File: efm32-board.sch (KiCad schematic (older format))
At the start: 30 parts, among them J1 Conn_01x20, J2 Conn_01x20, J3 USB_OTG, J4 Conn_02x03_Odd_Even, J5 Conn_01x20, J6 Conn_01x20, SW1 reset, SW2 reset, U1 EFM32HG-48LQFP, U2 SPX3819M5-L-3-3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

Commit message: Add +5v input diode array for split vbus and vin
Signed-off-by: Martin Ribelotta <martinribelotta@gmail.com>
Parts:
- added D2: PMEG2005CT, TO_SOT_Packages_SMD:SOT-23, symbol D_Schottky_x2_KCom_AAK
- J4: footprint Pin_Headers:Pin_Header_Straight_2x03_Pitch2.54mm_SMD -> Pin_Headers:Pin_Header_Straight_2x03_Pitch2.54mm
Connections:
- net +5V: now also D2.3 (K); no longer J2.1 (Pin_1), J3.1 (VBUS), J5.1 (Pin_1)
- new net vin: D2.1 (A), J2.1 (Pin_1), J5.1 (Pin_1)
- new net vusb: D2.2 (A), J3.1 (VBUS)

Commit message: Corrections and fixeds
Signed-off-by: Martin Ribelotta <martinribelotta@gmail.com>
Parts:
- added C12: 4.7u, Capacitors_SMD:C_0603, symbol C_Small
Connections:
- net +3V3: no longer C7.1, U1.33 (USB_VREGI), U1.34 (USB_VREGO)
- net +5V: no longer J4.2 (Pin_2)
- net GND: now also C12.2
- net vusb: now also U1.33 (USB_VREGI), C12.1
- new net: C7.1, U1.34 (USB_VREGO)
- no-connect marks 3 -> 4
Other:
- moved on the sheet: C7
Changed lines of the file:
@@
 L GND #PWR012
 U 1 1 59CF2E8C
-P 6450 3125
-F 0 "#PWR012" H 6450 2875 50  0001 C CNN
-F 1 "GND" H 6455 2952 50  0000 C CNN
-F 2 "" H 6450 3125 50  0001 C CNN
-F 3 "" H 6450 3125 50  0001 C CNN
-	1    6450 3125
+P 7000 3150
+F 0 "#PWR012" H 7000 2900 50  0001 C CNN
+F 1 "GND" H 7005 2977 50  0000 C CNN
+F 2 "" H 7000 3150 50  0001 C CNN
+F 3 "" H 7000 3150 50  0001 C CNN
+	1    7000 3150
 	1    0    0    -1
 $EndComp
@@
 L C_Small C7
 U 1 1 59CF2D3A
-P 6450 3000
-F 0 "C7" H 6542 3046 50  0000 L CNN
-F 1 "1u" H 6542 2955 50  0000 L CNN
-F 2 "Capacitors_SMD:C_0603" H 6450 3000 50  0001 C CNN
-F 3 "" H 6450 3000 50  0001 C CNN
-	1    6450 3000
+P 7000 3025
+F 0 "C7" H 7092 3071 50  0000 L CNN
+F 1 "1u" H 7092 2980 50  0000 L CNN
+F 2 "Capacitors_SMD:C_0603" H 7000 3025 50  0001 C CNN
+F 3 "" H 7000 3025 50  0001 C CNN
+	1    7000 3025
 	1    0    0    -1
 $EndComp
@@
 $EndComp
 $Comp
-L +3.3V #PWR013
-U 1 1 59CFEC3C
-P 6525 2875
-F 0 "#PWR013" H 6525 2725 50  0001 C CNN
-F 1 "+3.3V" V 6525 3100 50  0000 C CNN
-F 2 "" H 6525 2875 50  0000 C CNN
-F 3 "" H 6525 2875 50  0000 C CNN
-	1    6525 2875
-	0    1    1    0
-$EndComp
-$Comp
 L +3.3V #PWR06
 U 1 1 59CFED05
@@
 F 3 "" H 9775 4125 50  0000 C CNN
 	1    9775 4125
-	0    1    -1   0
-$EndComp
-$Comp
-L +5V #PWR024
-U 1 1 59D06FF8
-P 9775 4025
-F 0 "#PWR024" H 9775 3875 50  0001 C CNN
-F 1 "+5V" V 9775 4150 50  0000 L CNN
-F 2 "" H 9775 4025 50  0001 C CNN
-F 3 "" H 9775 4025 50  0001 C CNN
-	1    9775 4025
 	0    1    -1   0
 $EndComp
@@
 	6125 3475 6775 3475
 Wire Wire Line
-	6450 2875 6450 2900
-Connection ~ 6450 2875
-Wire Wire Line
-	6125 2975 6250 2975
-Wire Wire Line
-	6250 2975 6250 2875
-Connection ~ 6250 2875
-Wire Wire Line
 	6750 3475 6750 3525
 Connection ~ 6750 3475
@@
 	6125 3375 7200 3375
 Wire Wire Line
-	6125 2875 6525 2875
-Wire Wire Line
-	6450 3100 6450 3125
+	7000 3125 7000 3150
 Wire Wire Line
 	3050 3075 3050 3225
@@
 Wire Wire Line
 	7200 3375 7200 3400
-Wire Wire Line
-	9775 4025 9675 4025
 Wire Wire Line
 	9775 4125 9675 4125
@@
 	0    -1   -1   0
 $EndComp
+$Comp
+L GND #PWR013
+U 1 1 59D2EB13
+P 6675 3150
+F 0 "#PWR013" H 6675 2900 50  0001 C CNN
+F 1 "GND" H 6680 2977 50  0000 C CNN
+F 2 "" H 6675 3150 50  0001 C CNN
+F 3 "" H 6675 3150 50  0001 C CNN
+	1    6675 3150
+	1    0    0    -1
+$EndComp
+$Comp
+L C_Small C12
+U 1 1 59D2EB19
+P 6675 3025
+F 0 "C12" H 6767 3071 50  0000 L CNN
+F 1 "4.7u" H 6767 2980 50  0000 L CNN
+F 2 "Capacitors_SMD:C_0603" H 6675 3025 50  0001 C CNN
+F 3 "" H 6675 3025 50  0001 C CNN
+	1    6675 3025
+	1    0    0    -1
+$EndComp
+Wire Wire Line
+	6675 3125 6675 3150
+Wire Wire Line
+	6125 2975 6400 2975
+Wire Wire Line
+	6400 2975 6400 2925
+Wire Wire Line
+	6400 2925 6675 2925
+Wire Wire Line
+	6125 2875 7000 2875
+Wire Wire Line
+	7000 2875 7000 2925
+Text Label 6525 2800 0    60   ~ 0
+vusb
+Wire Wire Line
+	6525 2800 6525 2925
+Connection ~ 6525 2925
+NoConn ~ 9675 4025
 $EndSCHEMATC

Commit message: Add jump to pins 2-4 on J4 (SWD)
Signed-off-by: Martin Ribelotta <martinribelotta@gmail.com>
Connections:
- net +3V3: now also J4.2 (Pin_2)
- no-connect marks 4 -> 3
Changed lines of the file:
@@
 	6525 2800 6525 2925
 Connection ~ 6525 2925
-NoConn ~ 9675 4025
+Wire Wire Line
+	9675 4025 9725 4025
+Wire Wire Line
+	9725 4025 9725 4125
+Connection ~ 9725 4125
 $EndSCHEMATC

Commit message: Change usb resistors from 22R to 15R
Signed-off-by: Martin Ribelotta <martinribelotta@gmail.com>
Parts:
- R1, R2: value 22R -> 15R
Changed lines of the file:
@@
 P 7825 5350
 F 0 "R1" V 7675 5350 50  0000 C CNN
-F 1 "22R" V 7750 5350 50  0000 C CNN
+F 1 "15R" V 7750 5350 50  0000 C CNN
 F 2 "Resistors_SMD:R_0603" H 7825 5350 50  0001 C CNN
 F 3 "" H 7825 5350 50  0001 C CNN
@@
 P 7825 5550
 F 0 "R2" V 7975 5550 50  0000 C CNN
-F 1 "22R" V 7900 5550 50  0000 C CNN
+F 1 "15R" V 7900 5550 50  0000 C CNN
 F 2 "Resistors_SMD:R_0603" H 7825 5550 50  0001 C CNN
 F 3 "" H 7825 5550 50  0001 C CNN

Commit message: Various fixes for release
Signed-off-by: Martin Ribelotta <martinribelotta@gmail.com>
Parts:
- removed J4: Conn_02x03_Odd_Even, Pin_Headers:Pin_Header_Straight_2x03_Pitch2.54mm, symbol Conn_02x03_Odd_Even
- added J4: SWD, Pin_Headers:Pin_Header_Straight_2x02_Pitch2.54mm_SMD, symbol Conn_02x02_Odd_Even
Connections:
- net +3V3: now also J2.3 (Pin_3), J5.3 (Pin_3); no longer J2.2 (Pin_2), J5.2 (Pin_2)
- net GND: now also J2.2 (Pin_2), J5.2 (Pin_2), J4.2 (Pin_2); no longer J2.3 (Pin_3), J5.3 (Pin_3)
- net PF0/SWCLK: now also J4.1 (Pin_1)
- net PF1/SWDIO: now also J4.3 (Pin_3)
- net nRESET: now also J4.4 (Pin_4)
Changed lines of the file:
@@
-$EndComp
-$Comp
-L +3.3V #PWR025
-U 1 1 59D06FF2
-P 9775 4125
-F 0 "#PWR025" H 9775 3975 50  0001 C CNN
-F 1 "+3.3V" V 9775 4350 50  0000 C CNN
-F 2 "" H 9775 4125 50  0000 C CNN
-F 3 "" H 9775 4125 50  0000 C CNN
-	1    9775 4125
-	0    1    -1   0
 $EndComp
 $Comp
@@
 L GND #PWR026
 U 1 1 59D0712A
-P 9175 3300
-F 0 "#PWR026" H 9175 3050 50  0001 C CNN
-F 1 "GND" V 9180 3172 50  0000 R CNN
-F 2 "" H 9175 3300 50  0001 C CNN
-F 3 "" H 9175 3300 50  0001 C CNN
-	1    9175 3300
-	0    -1   1    0
+P 9175 3400
+F 0 "#PWR026" H 9175 3150 50  0001 C CNN
+F 1 "GND" V 9180 3272 50  0000 R CNN
+F 2 "" H 9175 3400 50  0001 C CNN
+F 3 "" H 9175 3400 50  0001 C CNN
+	1    9175 3400
+	0    -1   -1   0
 $EndComp
 $Comp
@@
 Text Label 9700 5500 3    60   ~ 0
 B_USB-
-Text Label 9175 4125 2    60   ~ 0
+Text Label 9675 4225 0    60   ~ 0
 PF1/SWDIO
-Text Label 9175 4025 2    60   ~ 0
+Text Label 9675 4125 0    60   ~ 0
 PF0/SWCLK
 $Comp
 L GND #PWR020
 U 1 1 59D13134
-P 9750 4225
-F 0 "#PWR020" H 9750 3975 50  0001 C CNN
-F 1 "GND" V 9755 4097 50  0000 R CNN
-F 2 "" H 9750 4225 50  0001 C CNN
-F 3 "" H 9750 4225 50  0001 C CNN
-	1    9750 4225
-	0    -1   -1   0
+P 9100 4125
+F 0 "#PWR020" H 9100 3875 50  0001 C CNN
+F 1 "GND" V 9105 3997 50  0000 R CNN
+F 2 "" H 9100 4125 50  0001 C CNN
+F 3 "" H 9100 4125 50  0001 C CNN
+	1    9100 4125
+	-1   0    0    1
 $EndComp
 Text Label 950  2600 0    60   ~ 0
@@
 nRESET
 $Comp
-L Conn_02x03_Odd_Even J4
-U 1 1 59D16554
-P 9375 4125
-F 0 "J4" H 9425 4442 50  0000 C CNN
-F 1 "Conn_02x03_Odd_Even" H 9425 4351 50  0000 C CNN
-F 2 "Pin_Headers:Pin_Header_Straight_2x03_Pitch2.54mm" H 9375 4125 50  0001 C CNN
-F 3 "" H 9375 4125 50  0001 C CNN
-	1    9375 4125
-	1    0    0    -1
-$EndComp
-$Comp
 L +3.3V #PWR032
 U 1 1 59D15100
-P 9175 3400
-F 0 "#PWR032" H 9175 3250 50  0001 C CNN
-F 1 "+3.3V" V 9175 3625 50  0000 C CNN
-F 2 "" H 9175 3400 50  0000 C CNN
-F 3 "" H 9175 3400 50  0000 C CNN
-	1    9175 3400
-	0    1    1    0
+P 9175 3300
+F 0 "#PWR032" H 9175 3150 50  0001 C CNN
+F 1 "+3.3V" V 9175 3525 50  0000 C CNN
+F 2 "" H 9175 3300 50  0000 C CNN
+F 3 "" H 9175 3300 50  0000 C CNN
+	1    9175 3300
+	0    1    -1   0
 $EndComp
 $Comp
 L GND #PWR021
 U 1 1 59D15A44
-P 1050 3200
-F 0 "#PWR021" H 1050 2950 50  0001 C CNN
-F 1 "GND" V 1055 3072 50  0000 R CNN
-F 2 "" H 1050 3200 50  0001 C CNN
-F 3 "" H 1050 3200 50  0001 C CNN
-	1    1050 3200
-	0    -1   1    0
+P 1050 3300
+F 0 "#PWR021" H 1050 3050 50  0001 C CNN
+F 1 "GND" V 1055 3172 50  0000 R CNN
+F 2 "" H 1050 3300 50  0001 C CNN
+F 3 "" H 1050 3300 50  0001 C CNN
+	1    1050 3300
+	0    -1   -1   0
 $EndComp
 $Comp
 L +3.3V #PWR029
 U 1 1 59D15A4B
-P 1050 3300
-F 0 "#PWR029" H 1050 3150 50  0001 C CNN
-F 1 "+3.3V" V 1050 3525 50  0000 C CNN
-F 2 "" H 1050 3300 50  0000 C CNN
-F 3 "" H 1050 3300 50  0000 C CNN
-	1    1050 3300
-	0    1    1    0
+P 1050 3200
+F 0 "#PWR029" H 1050 3050 50  0001 C CNN
+F 1 "+3.3V" V 1050 3425 50  0000 C CNN
+F 2 "" H 1050 3200 50  0000 C CNN
+F 3 "" H 1050 3200 50  0000 C CNN
+	1    1050 3200
+	0    1    -1   0
 $EndComp
 $Comp
@@
 	7200 3375 7200 3400
 Wire Wire Line
-	9775 4125 9675 4125
-Wire Wire Line
 	9275 1800 9075 1800
 Wire Wire Line
-	9075 3300 9175 3300
+	9075 3400 9175 3400
 Wire Wire Line
 	7225 1050 7000 1050
@@
 Connection ~ 1050 1600
 Wire Wire Line
-	9750 4225 9675 4225
+	9100 4125 9175 4125
 Wire Wire Line
 	9175 3500 9075 3500
 Wire Wire Line
-	9175 3400 9075 3400
-Wire Wire Line
-	950  3200 1050 3200
+	9175 3300 9075 3300
+Wire Wire Line
+	950  3300 1050 3300
 Wire Wire Line
 	1050 3400 950  3400
 Wire Wire Line
-	1050 3300 950  3300
+	1050 3200 950  3200
 Wire Wire Line
 	9075 850  9050 850
@@
 	6525 2800 6525 2925
 Connection ~ 6525 2925
-Wire Wire Line
-	9675 4025 9725 4025
-Wire Wire Line
-	9725 4025 9725 4125
-Connection ~ 9725 4125
+$Comp
+L Conn_02x02_Odd_Even J4
+U 1 1 59D30EE7
+P 9475 4125
+F 0 "J4" H 9525 4342 50  0000 C CNN
+F 1 "SWD" H 9525 4251 50  0000 C CNN
+F 2 "Pin_Headers:Pin_Header_Straight_2x02_Pitch2.54mm_SMD" H 9475 4125 50  0001 C CNN
+F 3 "" H 9475 4125 50  0001 C CNN
+	1    9475 4125
+	-1   0    0    -1
+$EndComp
 $EndSCHEMATC

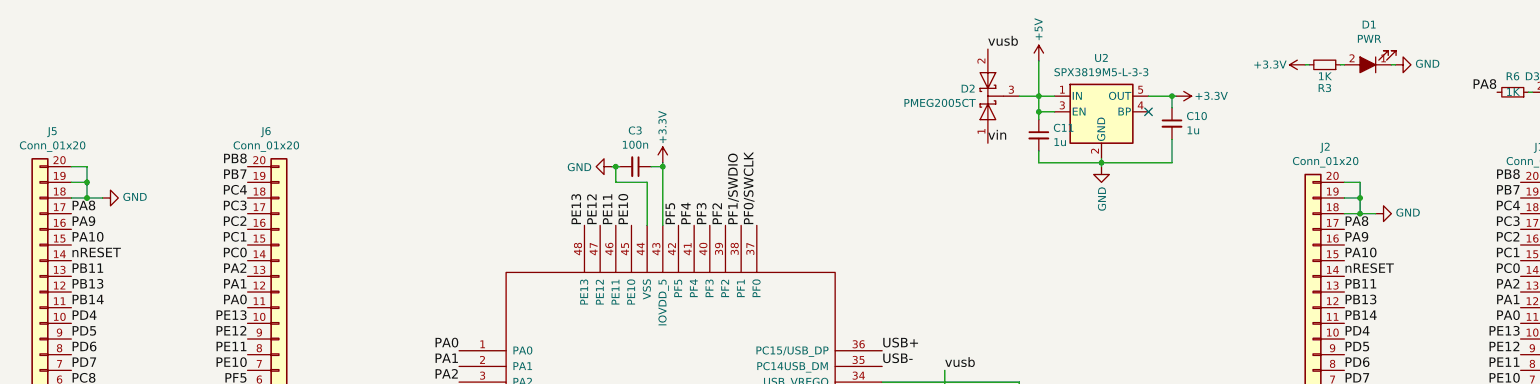
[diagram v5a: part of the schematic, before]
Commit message: Add +3v3 on pin 18 (previous GND) for prototyping convenience
Signed-off-by: Martin Ribelotta <martinribelotta@gmail.com>
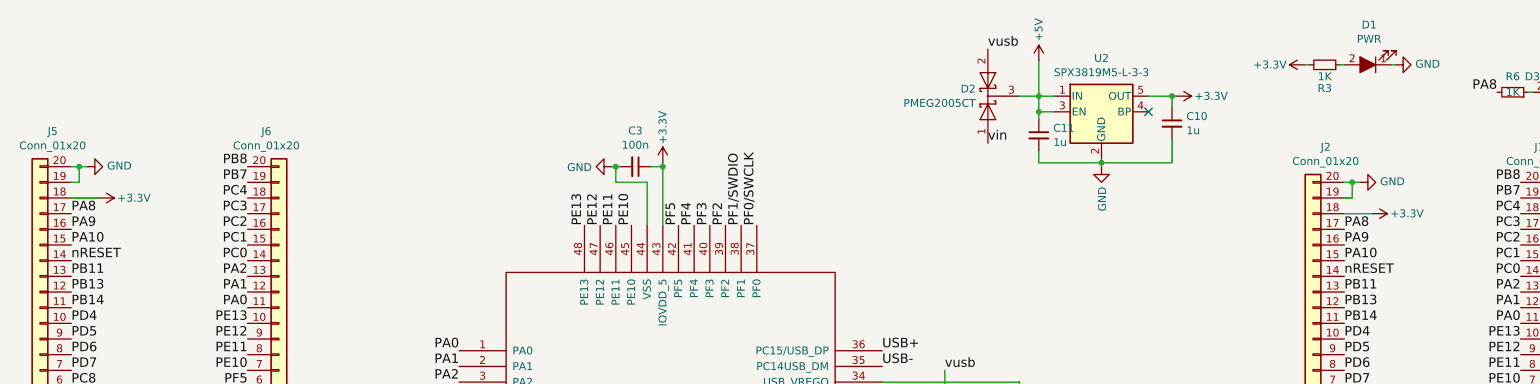
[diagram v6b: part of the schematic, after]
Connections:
- net +3V3: now also J2.18 (Pin_18), J5.18 (Pin_18)
- net GND: no longer J2.18 (Pin_18), J5.18 (Pin_18)
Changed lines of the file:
@@
-$EndComp
-$Comp
-L GND #PWR022
-U 1 1 59D07091
-P 9275 1800
-F 0 "#PWR022" H 9275 1550 50  0001 C CNN
-F 1 "GND" V 9280 1672 50  0000 R CNN
-F 2 "" H 9275 1800 50  0001 C CNN
-F 3 "" H 9275 1800 50  0001 C CNN
-	1    9275 1800
-	0    -1   -1   0
 $EndComp
 $Comp
@@
 L GND #PWR031
 U 1 1 59D1427A
-P 1150 1700
-F 0 "#PWR031" H 1150 1450 50  0001 C CNN
-F 1 "GND" V 1155 1572 50  0000 R CNN
-F 2 "" H 1150 1700 50  0001 C CNN
-F 3 "" H 1150 1700 50  0001 C CNN
-	1    1150 1700
+P 1050 1500
+F 0 "#PWR031" H 1050 1250 50  0001 C CNN
+F 1 "GND" V 1055 1372 50  0000 R CNN
+F 2 "" H 1050 1500 50  0001 C CNN
+F 3 "" H 1050 1500 50  0001 C CNN
+	1    1050 1500
 	0    -1   -1   0
 $EndComp
@@
 	7200 3375 7200 3400
 Wire Wire Line
-	9275 1800 9075 1800
-Wire Wire Line
 	9075 3400 9175 3400
 Wire Wire Line
@@
 Wire Wire Line
 	2700 5175 2700 5100
-Wire Wire Line
-	9075 1700 9175 1700
-Wire Wire Line
-	9175 1600 9175 1800
-Connection ~ 9175 1800
-Wire Wire Line
-	9075 1600 9175 1600
-Connection ~ 9175 1700
-Wire Wire Line
-	1150 1700 950  1700
-Wire Wire Line
-	950  1600 1050 1600
-Wire Wire Line
-	1050 1500 1050 1700
-Connection ~ 1050 1700
-Wire Wire Line
-	950  1500 1050 1500
-Connection ~ 1050 1600
 Wire Wire Line
 	9100 4125 9175 4125
@@
 	-1   0    0    -1
 $EndComp
+Wire Wire Line
+	1050 1500 950  1500
+Wire Wire Line
+	950  1600 1000 1600
+Wire Wire Line
+	1000 1600 1000 1500
+Connection ~ 1000 1500
+$Comp
+L +3.3V #PWR015
+U 1 1 59D31653
+P 1125 1700
+F 0 "#PWR015" H 1125 1550 50  0001 C CNN
+F 1 "+3.3V" V 1125 1925 50  0000 C CNN
+F 2 "" H 1125 1700 50  0000 C CNN
+F 3 "" H 1125 1700 50  0000 C CNN
+	1    1125 1700
+	0    1    -1   0
+$EndComp
+Wire Wire Line
+	1125 1700 950  1700
+$Comp
+L GND #PWR?
+U 1 1 59D31AB4
+P 9175 1600
+F 0 "#PWR?" H 9175 1350 50  0001 C CNN
+F 1 "GND" V 9180 1472 50  0000 R CNN
+F 2 "" H 9175 1600 50  0001 C CNN
+F 3 "" H 9175 1600 50  0001 C CNN
+	1    9175 1600
+	0    -1   -1   0
+$EndComp
+Wire Wire Line
+	9175 1600 9075 1600
+Wire Wire Line
+	9075 1700 9125 1700
+Wire Wire Line
+	9125 1700 9125 1600
+Connection ~ 9125 1600
+$Comp
+L +3.3V #PWR?
+U 1 1 59D31ABE
+P 9250 1800
+F 0 "#PWR?" H 9250 1650 50  0001 C CNN
+F 1 "+3.3V" V 9250 2025 50  0000 C CNN
+F 2 "" H 9250 1800 50  0000 C CNN
+F 3 "" H 9250 1800 50  0000 C CNN
+	1    9250 1800
+	0    1    -1   0
+$EndComp
+Wire Wire Line
+	9250 1800 9075 1800
 $EndSCHEMATC
